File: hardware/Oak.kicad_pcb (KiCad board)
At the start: 2 copper layers, 100 x 40 mm, 73 parts, among them J1 18650 Battery holder, J2 USB_B_Micro, J3 Conn_Coaxial, J4 Conn_ARM_JTAG_SWD_10, SW1 SW_SPDT, SW2 SW_Push, U1 AP2112, U2 ATSAMD21, U3 MCP7383, U4 PA1010D, U5 RFM95, U6 Waveshare_1in54_epaper

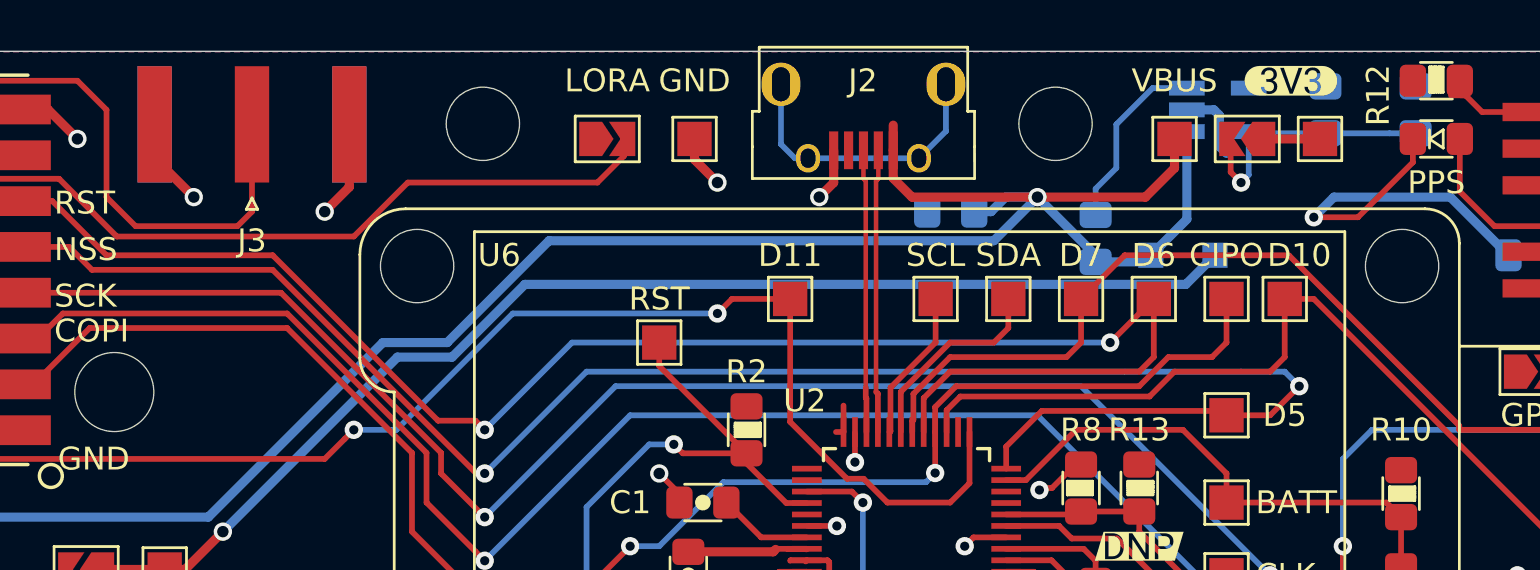
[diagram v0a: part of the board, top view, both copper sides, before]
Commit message: fix: change SMA connector to 0.25 inch
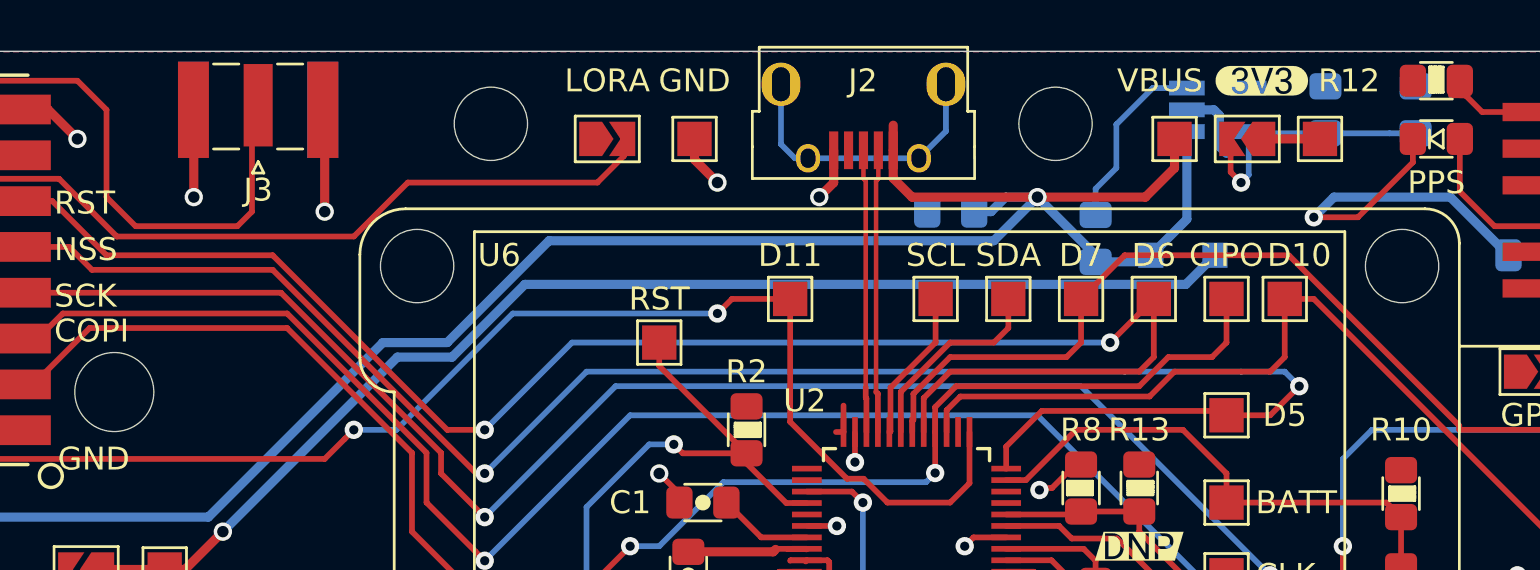
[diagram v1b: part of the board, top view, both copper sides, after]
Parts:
- J3: footprint Connector_Coaxial:SMA_Amphenol_132289_EdgeMount -> Connector_Coaxial:SMA_Samtec_SMA-J-P-X-ST-EM1_EdgeMount
- moved svg2mod 1.27 mm to (95.2, 34.3)
- moved J3 0.69 mm to (51.4, 35.6), turned to 180 degrees
- moved REF** 0.35 mm to (61.6, 36.2)
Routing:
- net Net-(J3-Pad1): track 34.2 -> 35.2 mm

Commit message: chore: update all images and docs
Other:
- board text added: "Oak@Hutscape V1.1 June 2021"
- board text removed: "Oak@Hutscape V1.0 June 2021"

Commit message: refactor: regenerate drill map files
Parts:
- moved D2 15.9 mm to (45.5, 57.1)
- moved REF** 15.9 mm to (44.5, 66.2)
- moved C1 15.9 mm to (86.7, 51.4)
- moved C10 15.9 mm to (97.5, 38.7)
- moved C11 15.9 mm to (53.1, 54.0)
- moved C2 15.9 mm to (93.7, 59.7)
- moved C3 15.9 mm to (86.1, 54.6)
- moved C4 15.9 mm to (103.9, 55.9)
- moved C5 15.9 mm to (53.1, 57.1)
- moved C6 15.9 mm to (113.9, 34.3)
- moved C7 15.9 mm to (117.8, 34.3)
- moved C9 15.9 mm to (55.6, 57.1)
- moved D1 15.9 mm to (107.7, 40.6)
- moved D3 15.9 mm to (118.7, 35.6)
- moved D4 15.9 mm to (81.0, 66.0)
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
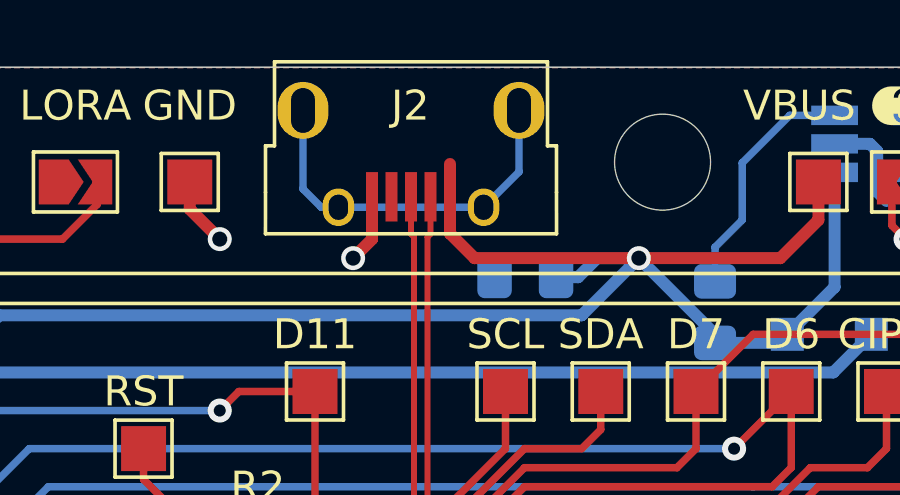
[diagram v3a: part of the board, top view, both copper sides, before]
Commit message: refactor: rotate symbol name and delete extra track on uUSB J2
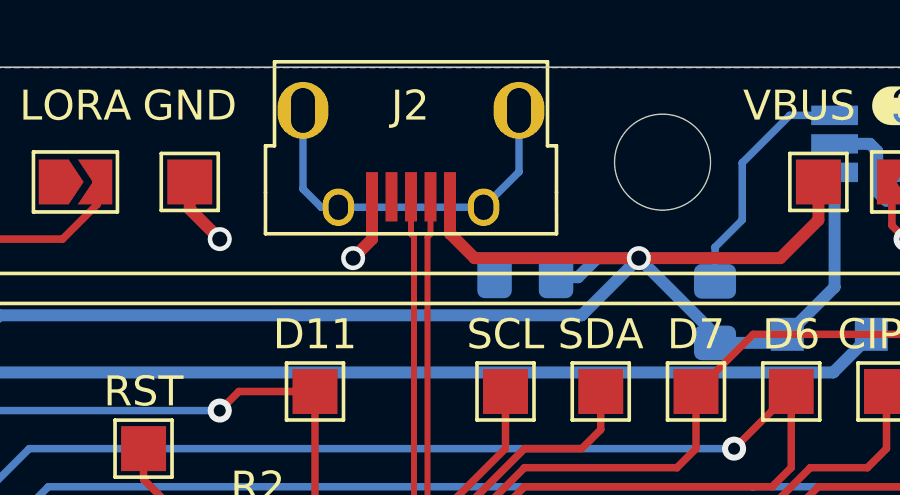
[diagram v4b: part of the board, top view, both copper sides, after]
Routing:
- net /VBUS: track 96.4 -> 95.3 mm

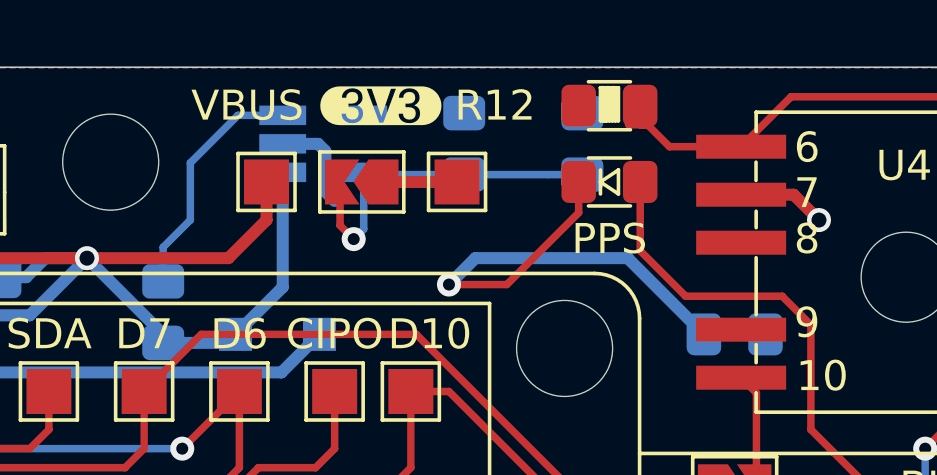
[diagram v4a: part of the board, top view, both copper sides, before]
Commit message: refactor: change track width to power net class for VOUT 3.3V of LDO
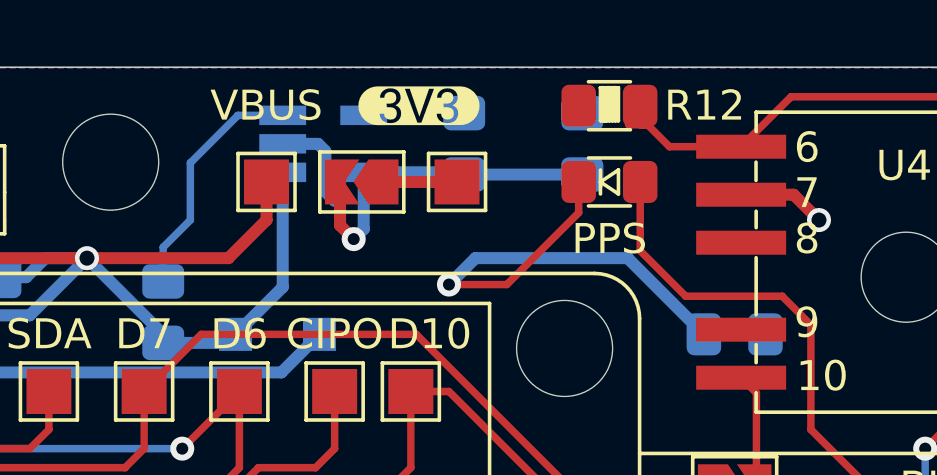
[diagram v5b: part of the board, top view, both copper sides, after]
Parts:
- moved svg2mod 1.27 mm to (112.4, 33.0)

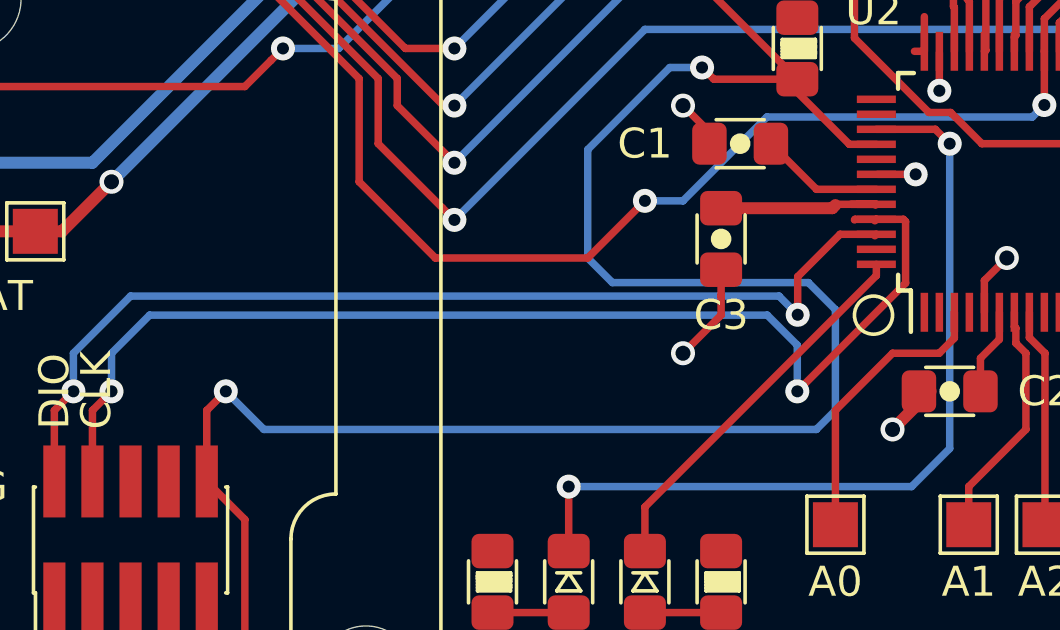
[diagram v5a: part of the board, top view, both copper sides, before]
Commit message: refactor: add RST on silkscreen for SWD connector and delete extra tracks on pads
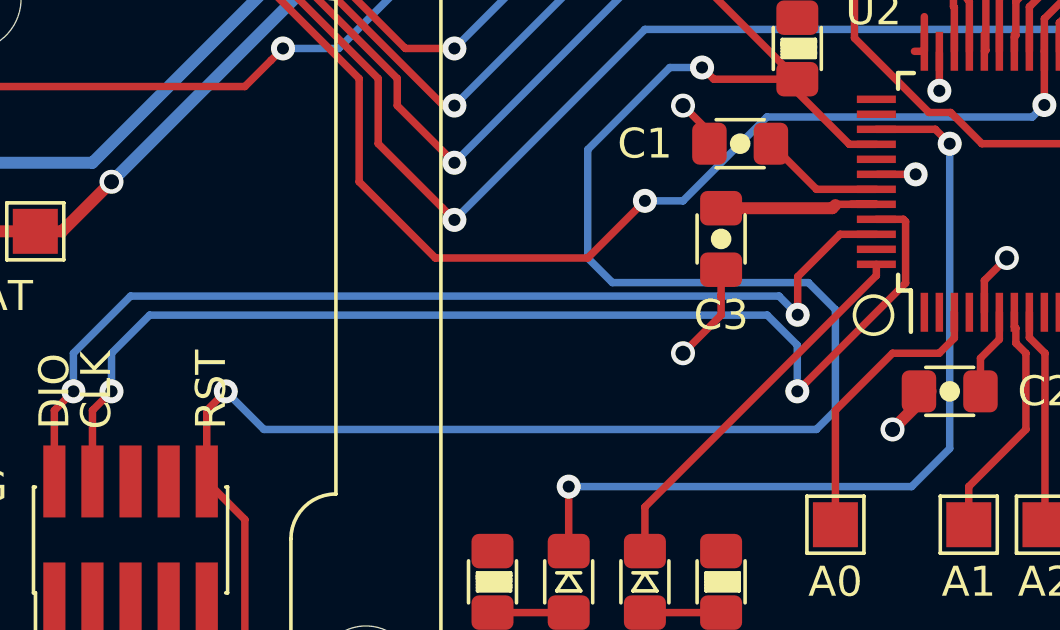
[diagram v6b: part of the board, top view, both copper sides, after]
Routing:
- net /SWCLK: track 38.8 -> 38.0 mm

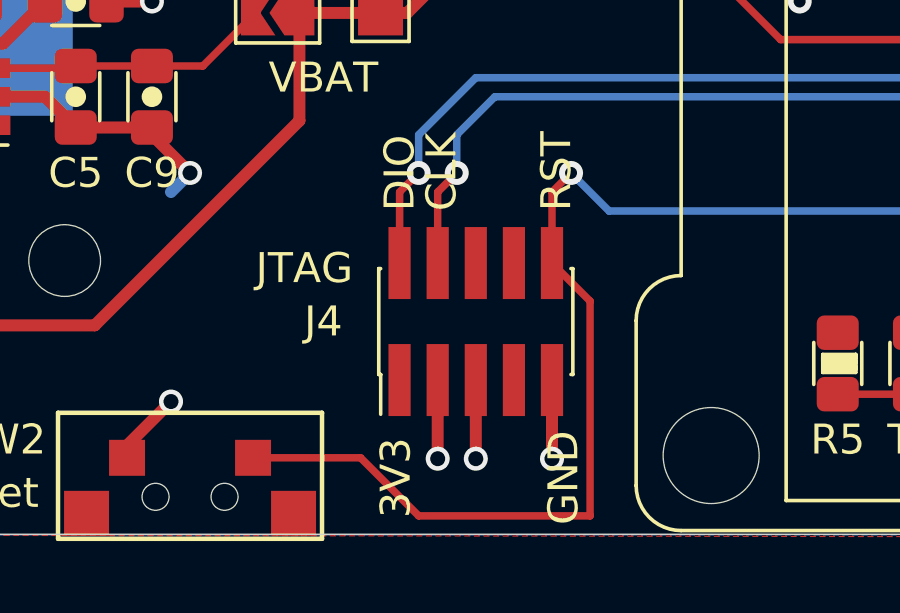
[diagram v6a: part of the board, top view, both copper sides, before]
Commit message: refactor: add an option to not connect Vtref for SWD for J-Link Edu mini
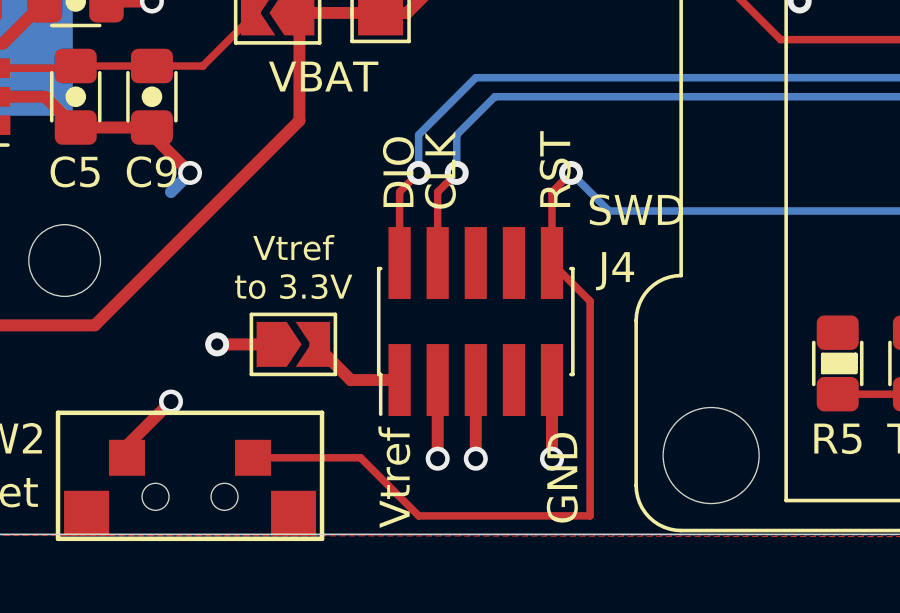
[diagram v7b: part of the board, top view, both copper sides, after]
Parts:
- added JP6: SolderJumper_2_Open, Jumper:SolderJumper-2_P1.3mm_Open_TrianglePad1.0x1.5mm, F.Cu at (60.3, 65.4)
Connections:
- J4 pad 1: +3V3 -> Net-(J4-Pad1)
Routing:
- net Net-(J4-Pad1): track 0.00 -> 3.31 mm
- net +3V3: track 18.5 -> 20.3 mm, vias 0 -> 1
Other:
- board text added: "Oak@Hutscape V1.2 July 2021"
- board text added: "SWD"
- board text added: "Vtref"
- board text added: "Vtref to 3.3V"
- board text removed: "3V3"
- board text removed: "JTAG"
- board text removed: "Oak@Hutscape V1.1 June 2021"
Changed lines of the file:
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@@
   (general
     (thickness 1.6)
-    (drawings 3562)
-    (tracks 607)
+    (drawings 3563)
+    (tracks 611)
     (zones 0)
-    (modules 73)
-    (nets 76)
+    (modules 74)
+    (nets 77)
   )
   (page A4)
   (title_block
     (title Oak)
-    (date 2021-05-31)
-    (rev V1.1)
+    (date 2021-07-02)
+    (rev V1.2)
     (company Hutscape)
-    (comment 1 "Description: Measure outdoor distance between 2 keychain holders")
+    (comment 1 "Description: Outdoor LoRa-GPS tracker with E-Ink display")
     (comment 2 "License: CC-BY-SA 4.0 or TAPR")
     (comment 3 "Project website: https://hutscape.com/oak")
@@
   (net 74 /GPS_TX)
   (net 75 /LORA_DATA)
+  (net 76 "Net-(J4-Pad1)")
   (net_class Default "This is the default net class."
     (clearance 0.2)
@@
     (uvia_dia 0.3)
     (uvia_drill 0.1)
+    (add_net +3V3)
     (add_net /A0)
     (add_net /A1)
@@
     (uvia_dia 0.3)
     (uvia_drill 0.1)
-    (add_net +3V3)
     (add_net /VBAT)
     (add_net /VBUS)
@@
     (add_net "Net-(C6-Pad1)")
     (add_net "Net-(J1-Pad1)")
+    (add_net "Net-(J4-Pad1)")
+  )
+  (module Jumper:SolderJumper-2_P1.3mm_Open_TrianglePad1.0x1.5mm (layer F.Cu)
+    (at 60.325 65.405)
+    (descr "SMD Solder Jumper, 1x1.5mm Triangular Pads, 0.3mm gap, open")
+    (tags "solder jumper open")
+    (attr virtual)
+    (fp_text reference JP6 (at -2.54 0 270) (layer F.SilkS) hide
+      (effects (font (size 1 1) (thickness 0.15)))
+    )
+    (fp_text value SolderJumper_2_Open (at 0 1.9) (layer F.Fab) hide
+      (effects (font (size 1 1) (thickness 0.15)))
+    )
+    (fp_line (start 1.65 1.25) (end -1.65 1.25) (layer F.CrtYd) (width 0.05))
+    (fp_line (start 1.65 1.25) (end 1.65 -1.25) (layer F.CrtYd) (width 0.05))
+    (fp_line (start -1.65 -1.25) (end -1.65 1.25) (layer F.CrtYd) (width 0.05))
+    (fp_line (start -1.65 -1.25) (end 1.65 -1.25) (layer F.CrtYd) (width 0.05))
+    (fp_line (start -1.4 -1) (end 1.4 -1) (layer F.SilkS) (width 0.12))
+    (fp_line (start 1.4 -1) (end 1.4 1) (layer F.SilkS) (width 0.12))
+    (fp_line (start 1.4 1) (end -1.4 1) (layer F.SilkS) (width 0.12))
+    (fp_line (start -1.4 1) (end -1.4 -1) (layer F.SilkS) (width 0.12))
+    (pad 1 smd custom (at -0.725 0) (size 0.3 0.3) (layers F.Cu F.Mask)
+      (net 3 +3V3) (zone_connect 2)
+      (options (clearance outline) (anchor rect))
+      (primitives
+        (gr_poly (pts
+           (xy -0.5 -0.75) (xy 0.5 -0.75) (xy 1 0) (xy 0.5 0.75) (xy -0.5 0.75)
+) (width 0))
+      ))
+    (pad 2 smd custom (at 0.725 0) (size 0.3 0.3) (layers F.Cu F.Mask)
+      (net 76 "Net-(J4-Pad1)") (zone_connect 2)
+      (options (clearance outline) (anchor rect))
+      (primitives
+        (gr_poly (pts
+           (xy -0.65 -0.75) (xy 0.5 -0.75) (xy 0.5 0.75) (xy -0.65 0.75) (xy -0.15 0)
+) (width 0))
+      ))
   )
   (module Connector_Coaxial:SMA_Samtec_SMA-J-P-X-ST-EM1_EdgeMount (layer F.Cu)
@@
     (tags "Surface mounted pin header SMD 2x05 1.27mm double row")
     (attr smd)
-    (fp_text reference J4 (at 0 -5.08 180) (layer F.SilkS)
+    (fp_text reference J4 (at 1.778 4.715 180) (layer F.SilkS)
       (effects (font (size 1 1) (thickness 0.15)))
     )
@@
       (net 21 /SWDIO))
     (pad 1 smd rect (at -1.95 -2.54 90) (size 2.4 0.74) (layers F.Cu F.Paste F.Mask)
-      (net 3 +3V3))
+      (net 76 "Net-(J4-Pad1)"))
     (model ${KISYS3DMOD}/Connector_PinHeader_1.27mm.3dshapes/PinHeader_2x05_P1.27mm_Vertical_SMD.wrl
       (at (xyz 0 0 0))
@@
       (net 26 /RST))
   )
+  (gr_text "Vtref\nto 3.3V" (at 60.325 62.865) (layer F.SilkS)
+    (effects (font (size 0.8 0.8) (thickness 0.15)))
+  )
   (gr_text RST (at 69.088 60.96 90) (layer F.SilkS)
     (effects (font (size 1 1) (thickness 0.15)) (justify left))
@@
   )
   (gr_circle (center 91.17 57.15) (end 91.678 57.531) (layer F.SilkS) (width 0.12))
-  (gr_text JTAG (at 60.69 62.865) (layer F.SilkS)
+  (gr_text SWD (at 71.755 60.96) (layer F.SilkS)
     (effects (font (size 1 1) (thickness 0.15)))
   )
@@
     (effects (font (size 1 1) (thickness 0.15)))
   )
-  (gr_text 3V3 (at 63.738 69.85 90) (layer F.SilkS)
+  (gr_text Vtref (at 63.738 69.85 90) (layer F.SilkS)
     (effects (font (size 1 1) (thickness 0.15)))
   )
@@
     (effects (font (size 1 1) (thickness 0.15)) (justify mirror))
   )
-  (gr_text "Oak@Hutscape V1.1 June 2021" (at 54.61 39.243) (layer B.SilkS)
+  (gr_text "Oak@Hutscape V1.2 July 2021" (at 54.61 39.243) (layer B.SilkS)
     (effects (font (size 1 1) (thickness 0.15)) (justify mirror))
   )
@@
   (segment (start 89.9 53.480011) (end 89.925011 53.455) (width 0.25) (layer F.Cu) (net 3))
   (segment (start 111.215 35.56) (end 113.665 35.56) (width 0.4) (layer F.Cu) (net 3))
+  (segment (start 59.6 65.405) (end 57.785 65.405) (width 0.4) (layer F.Cu) (net 3))
+  (via (at 57.785 65.405) (size 0.8) (drill 0.4) (layers F.Cu B.Cu) (net 3))
   (segment (start 52.995 56.2) (end 53.07 56.125) (width 0.25) (layer F.Cu) (net 4))
   (segment (start 50.36 56.2) (end 52.995 56.2) (width 0.25) (layer F.Cu) (net 4))
@@
   (segment (start 73.346019 48.26) (end 71.485 48.26) (width 0.25) (layer B.Cu) (net 75))
   (segment (start 87.36 43.18) (end 78.426019 43.18) (width 0.25) (layer B.Cu) (net 75))
+  (segment (start 62.238 66.593) (end 61.05 65.405) (width 0.4) (layer F.Cu) (net 76))
+  (segment (start 63.865 66.593) (end 62.238 66.593) (width 0.4) (layer F.Cu) (net 76))
   (zone (net 2) (net_name GND) (layer B.Cu) (hatch edge 0.508)
     (connect_pads (clearance 0.508))

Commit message: feat: add silkscreen writable area for LoRa node address and frequency. close #25
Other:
- board text added: "Frequency:"
- board text added: "MHz"
- board text added: "Node address: 0x"
